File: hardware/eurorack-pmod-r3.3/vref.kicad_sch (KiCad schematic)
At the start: 8 parts, among them U8 LM4040DBZ-3 VREF, U9 TL072 OP AMP

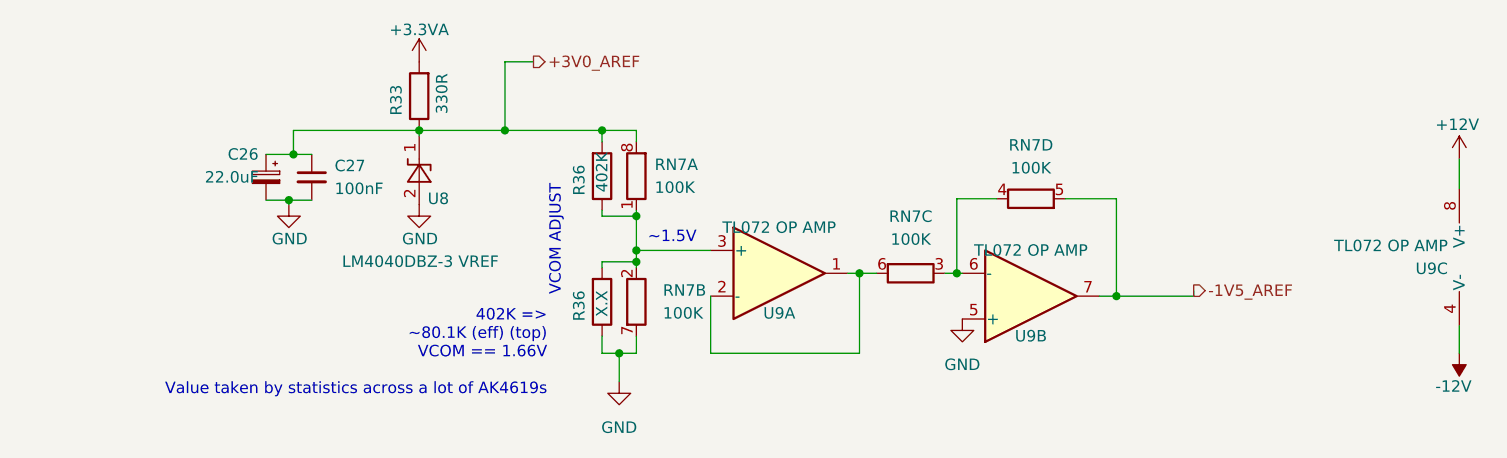
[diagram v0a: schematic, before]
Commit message: - Swap stackup s/4/6     - Was: GND/SIG/SIG/GND     - Now: GND/VDD/SIG/SIG/GND/GND - Swap CY8CMBR3108 for CY8CMBR3116     - Touch indices do NOT match previous revision.     - TODO revise new pinout (XRES) - Combine GNDD and GNDA     - Remove inductors between planes     - Mounting hole connects to GNDD / GNDA - Clean up traces now moved to VDD plane - Add EMC 33R series on SDOUT1
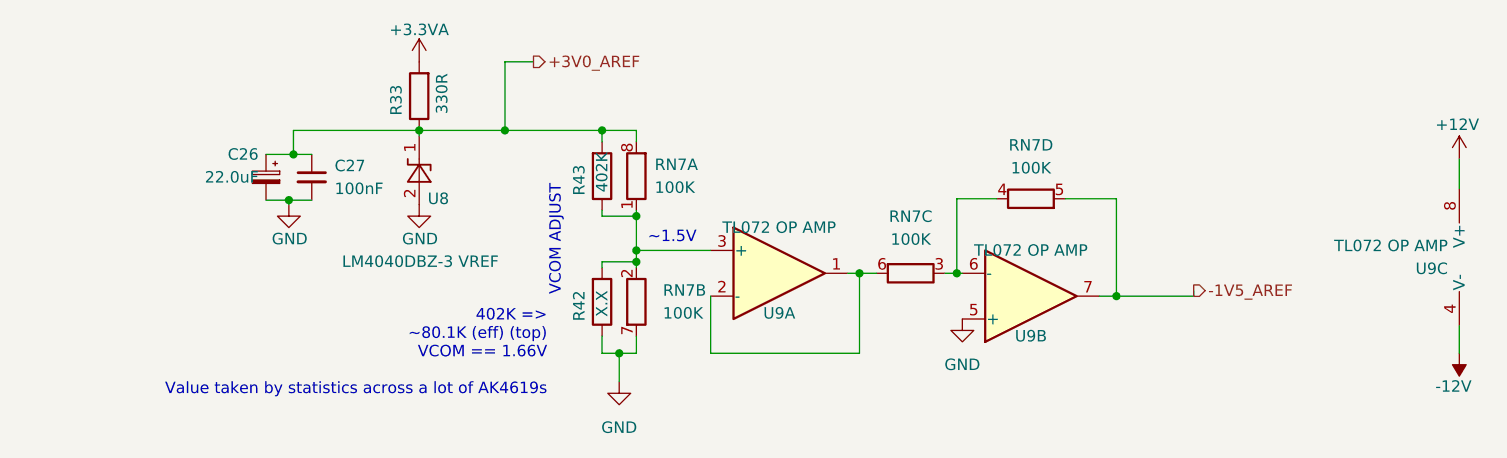
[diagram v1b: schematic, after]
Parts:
- renumbered R36 to R42, R36 to R43

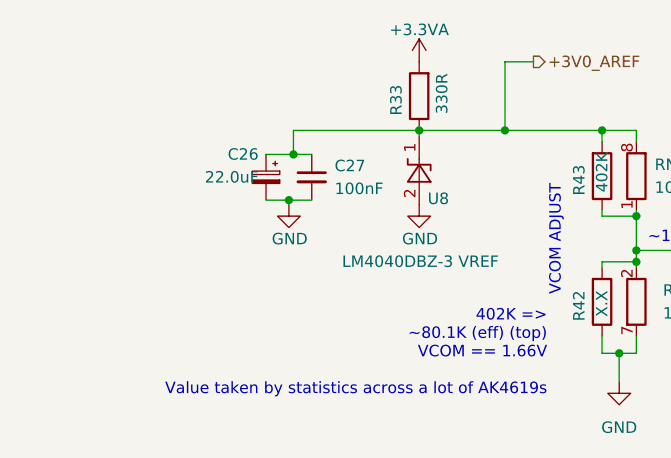
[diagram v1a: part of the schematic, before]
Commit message: - Swap all tantalums for ceramics
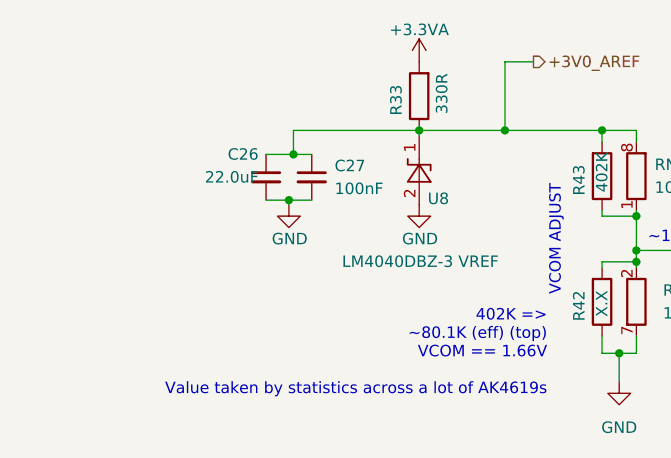
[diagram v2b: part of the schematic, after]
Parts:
- C26: footprint Capacitor_Tantalum_SMD:CP_EIA-3216-10_Kemet-I -> Capacitor_SMD:C_1206_3216Metric; symbol Device:C_Polarized_Small -> Device:C_Small; lcsc# C782264 -> C12891
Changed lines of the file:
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@@
 	)
 	(symbol
-		(lib_id "Device:C_Polarized_Small")
+		(lib_id "Device:C_Small")
 		(at 80.772 45.212 0)
 		(mirror y)
@@
 			)
 		)
-		(property "Footprint" "Capacitor_Tantalum_SMD:CP_EIA-3216-10_Kemet-I"
+		(property "Footprint" "Capacitor_SMD:C_1206_3216Metric"
 			(at 80.772 45.212 0)
 			(effects
@@
 			)
 		)
-		(property "Datasheet" ""
+		(property "Datasheet" "~"
 			(at 80.772 45.212 0)
 			(effects
@@
 			)
 		)
-		(property "Description" ""
+		(property "Description" "Unpolarized capacitor, small symbol"
 			(at 80.772 45.212 0)
 			(effects
@@
 					(size 1.27 1.27)
 				)
+				(hide yes)
 			)
 		)
@@
 			)
 		)
-		(property "lcsc#" "C782264"
+		(property "lcsc#" "C12891"
 			(at 80.772 45.212 0)
 			(effects

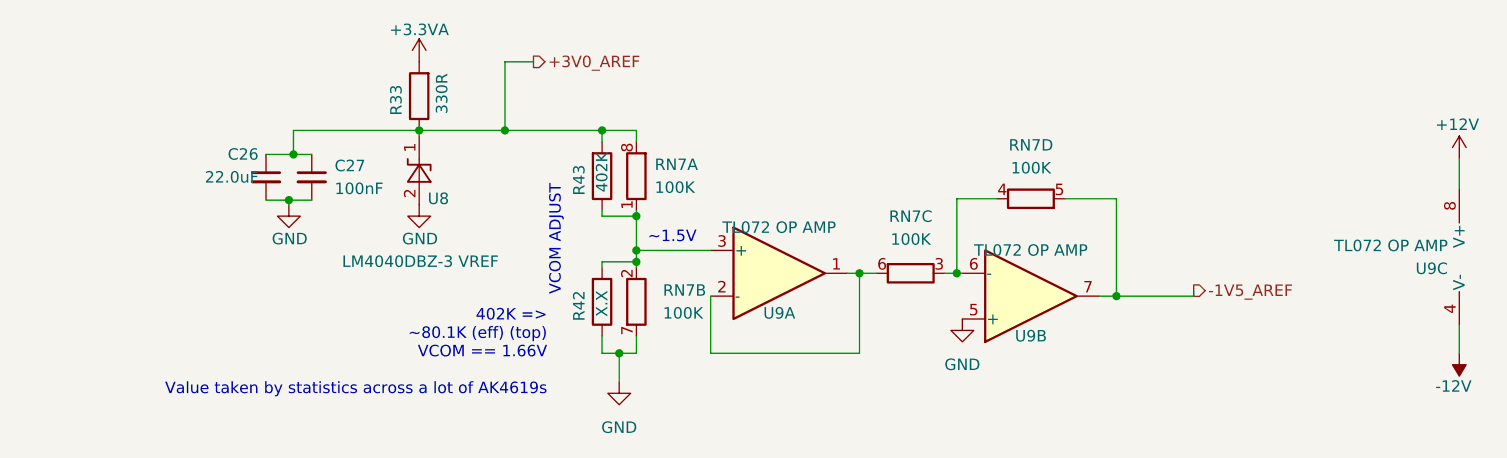
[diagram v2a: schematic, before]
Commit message: vref: replace +3.0V with local 12V->3.3V LDO
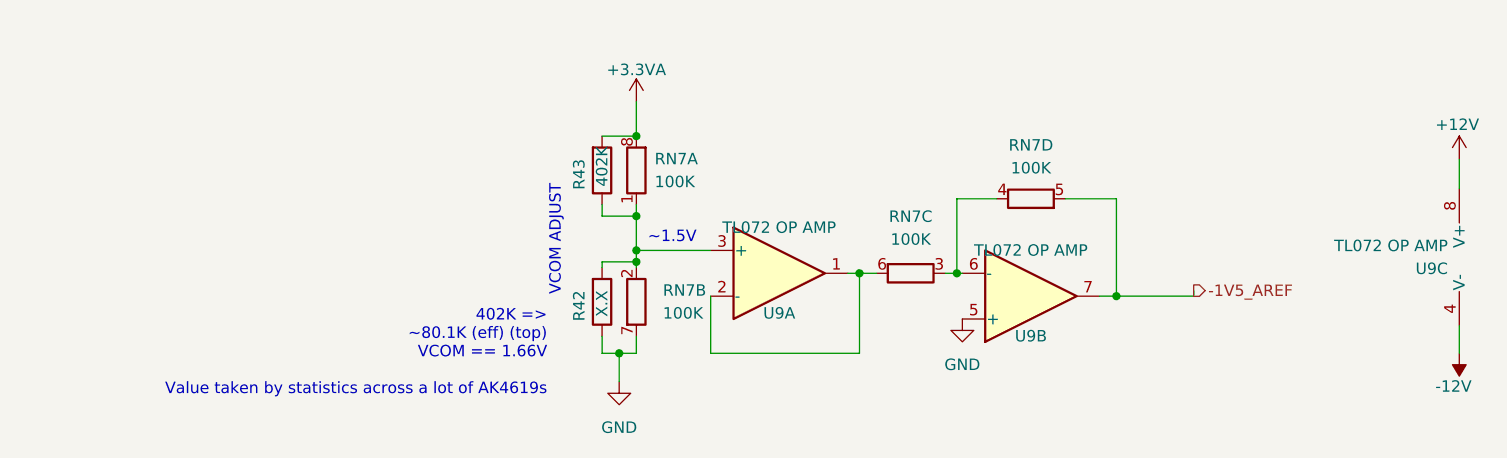
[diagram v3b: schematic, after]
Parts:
- removed C26: 22.0uF, Capacitor_SMD:C_1206_3216Metric, symbol Device:C_Small
- removed C27: 100nF, Capacitor_SMD:C_0603_1608Metric, symbol Device:C_Small
- removed R33: 330R, Resistor_SMD:R_0603_1608Metric, symbol Device:R
- removed U8: LM4040DBZ-3 VREF, Package_TO_SOT_SMD:SOT-23, symbol Reference_Voltage:LM4040DBZ-3
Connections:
- net +3V0_AREF is gone; now on net +3.3VA: R43.2, RN7.8 (R1.2)
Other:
- moved on the sheet: R43, RN7A

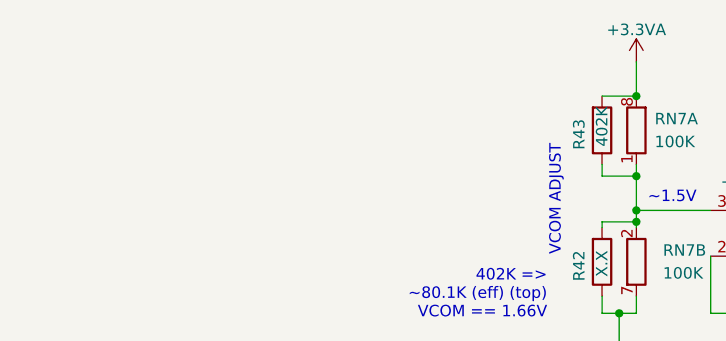
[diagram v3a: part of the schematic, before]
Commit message: place new parts
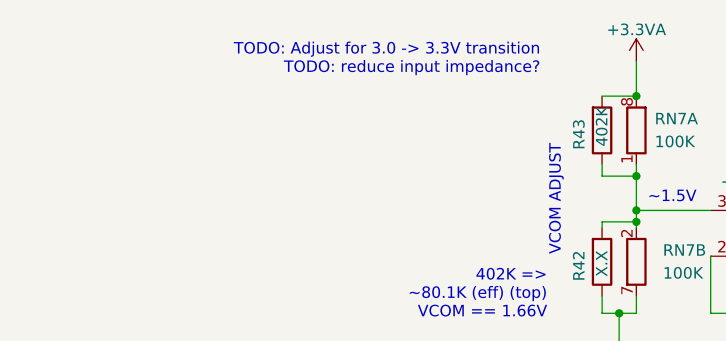
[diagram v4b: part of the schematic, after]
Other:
- note added: "TODO: Adjust for 3.0 -> 3.3V transition TODO: reduce input impedance?"
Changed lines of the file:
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@@
 	(generator_version "9.0")
 	(paper "A4")
+	(text "TODO: Adjust for 3.0 -> 3.3V transition\nTODO: reduce input impedance?"
+		(exclude_from_sim no)
+		(at 111.252 38.354 0)
+		(effects
+			(font
+				(size 1.27 1.27)
+			)
+			(justify right bottom)
+		)
+	)
 	(text "402K =>\n~80.1K (eff) (top)\nVCOM == 1.66V\n\nValue taken by statistics across a lot of AK4619s"
 		(exclude_from_sim no)

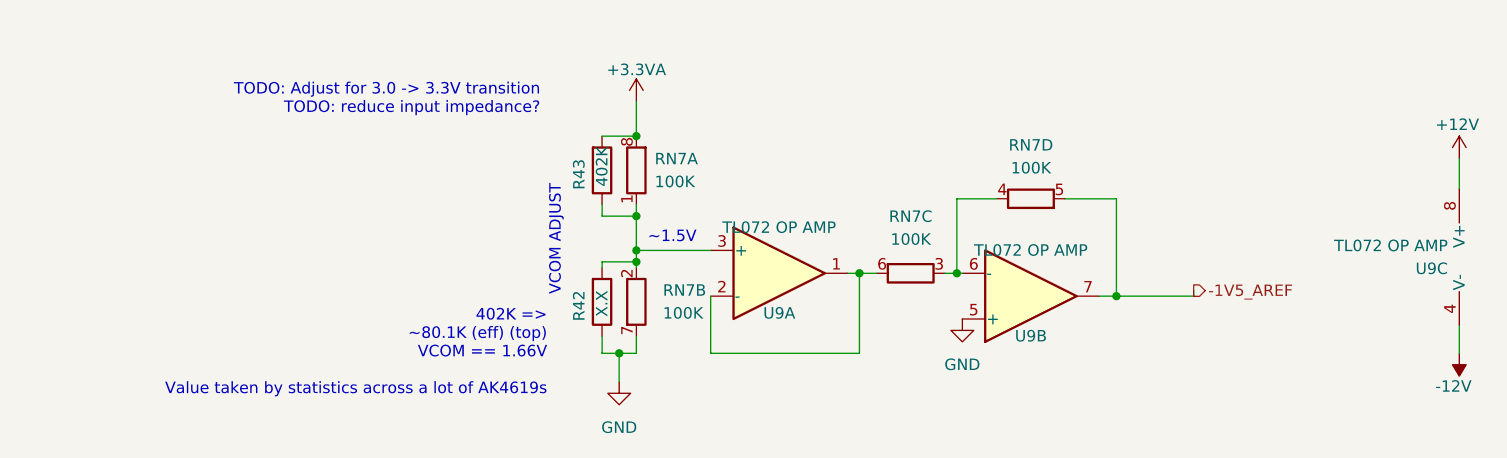
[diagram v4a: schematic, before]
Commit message: r3.5: add 100k output terminations and 100nF vref filtering, fab outputs (not sent yet)
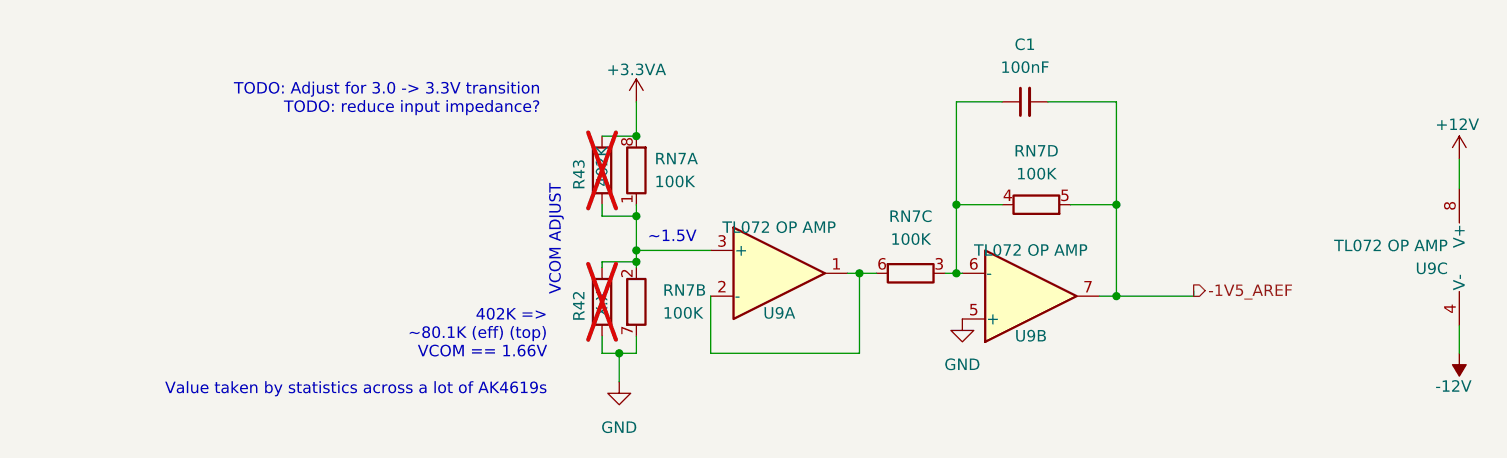
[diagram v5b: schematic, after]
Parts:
- added C1: 100nF, Capacitor_SMD:C_0603_1608Metric, symbol Device:C_Small
- R42, R43: now not fitted; now left out of the parts list
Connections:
- net -1V5_AREF: now also C1.2
- net at RN7.3 (R3.1), RN7.4 (R4.1), U9.6 (-): now also C1.1
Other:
- moved on the sheet: RN7D
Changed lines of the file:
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@@
+	)
+	(junction
+		(at 157.48 48.26)
+		(diameter 0)
+		(color 0 0 0 0)
 	)
 	(junction
@@
 	)
 	(junction
-		(at 121.92 53.34)
+		(at 157.48 55.88)
 		(diameter 0)
 		(color 0 0 0 0)
 	)
 	(junction
-		(at 157.5308 55.88)
+		(at 121.92 53.34)
 		(diameter 0)
 		(color 0 0 0 0)
@@
 		(color 0 0 0 0)
 	)
+	(junction
+		(at 175.26 48.26)
+		(diameter 0)
+		(color 0 0 0 0)
+	)
 	(wire
 		(pts
@@
 	(wire
 		(pts
+			(xy 162.56 36.83) (xy 157.48 36.83)
+		)
+		(stroke
+			(width 0)
+			(type default)
+		)
+	)
+	(wire
+		(pts
 			(xy 175.26 58.42) (xy 183.8452 58.42)
 		)
@@
 	(wire
 		(pts
+			(xy 157.48 36.83) (xy 157.48 48.26)
+		)
+		(stroke
+			(width 0)
+			(type default)
+		)
+	)
+	(wire
+		(pts
 			(xy 146.7104 55.88) (xy 148.59 55.88)
 		)
@@
 	(wire
 		(pts
+			(xy 175.26 36.83) (xy 175.26 48.26)
+		)
+		(stroke
+			(width 0)
+			(type default)
+		)
+	)
+	(wire
+		(pts
 			(xy 130.175 64.77) (xy 146.7104 64.77)
 		)
@@
 	(wire
 		(pts
+			(xy 167.64 36.83) (xy 175.26 36.83)
+		)
+		(stroke
+			(width 0)
+			(type default)
+		)
+	)
+	(wire
+		(pts
 			(xy 213.36 61.722) (xy 213.36 64.77)
 		)
@@
 	(wire
 		(pts
-			(xy 175.26 47.5996) (xy 175.26 58.42)
+			(xy 175.26 48.26) (xy 175.26 58.42)
 		)
 		(stroke
@@
 	(wire
 		(pts
+			(xy 157.48 55.88) (xy 158.1404 55.88)
+		)
+		(stroke
+			(width 0)
+			(type default)
+		)
+	)
+	(wire
+		(pts
 			(xy 173.3804 58.42) (xy 175.26 58.42)
 		)
@@
 	(wire
 		(pts
-			(xy 169.5704 47.5996) (xy 175.26 47.5996)
-		)
-		(stroke
-			(width 0)
-			(type default)
-		)
-	)
-	(wire
-		(pts
-			(xy 157.5308 55.88) (xy 158.1404 55.88)
+			(xy 170.18 48.26) (xy 175.26 48.26)
 		)
 		(stroke
@@
 	(wire
 		(pts
-			(xy 157.5308 47.5996) (xy 161.9504 47.5996)
-		)
-		(stroke
-			(width 0)
-			(type default)
-		)
-	)
-	(wire
-		(pts
-			(xy 156.21 55.88) (xy 157.5308 55.88)
+			(xy 157.48 48.26) (xy 162.56 48.26)
+		)
+		(stroke
+			(width 0)
+			(type default)
+		)
+	)
+	(wire
+		(pts
+			(xy 156.21 55.88) (xy 157.48 55.88)
 		)
 		(stroke
@@
 	(wire
 		(pts
-			(xy 157.5308 47.5996) (xy 157.5308 55.88)
+			(xy 157.48 48.26) (xy 157.48 55.88)
 		)
 		(stroke
@@
 		(unit 1)
 		(exclude_from_sim no)
-		(in_bom yes)
-		(on_board yes)
-		(dnp no)
+		(in_bom no)
+		(on_board no)
+		(dnp yes)
 		(property "Reference" "R42"
 			(at 115.57 57.785 90)
@@
 		(unit 1)
 		(exclude_from_sim no)
-		(in_bom yes)
-		(on_board yes)
-		(dnp no)
+		(in_bom no)
+		(on_board no)
+		(dnp yes)
 		(property "Reference" "R43"
 			(at 115.57 43.18 90)
@@
 	)
 	(symbol
+		(lib_id "Device:C_Small")
+		(at 165.1 36.83 90)
+		(mirror x)
+		(unit 1)
+		(exclude_from_sim no)
+		(in_bom yes)
+		(on_board yes)
+		(dnp no)
+		(fields_autoplaced yes)
+		(property "Reference" "C1"
+			(at 165.1063 30.48 90)
+			(effects
+				(font
+					(size 1.27 1.27)
+				)
+			)
+		)
+		(property "Value" "100nF"
+			(at 165.1063 33.02 90)
+			(effects
+				(font
+					(size 1.27 1.27)
+				)
+			)
+		)
+		(property "Footprint" "Capacitor_SMD:C_0603_1608Metric"
+			(at 165.1 36.83 0)
+			(effects
+				(font
+					(size 1.27 1.27)
+				)
+				(hide yes)
+			)
+		)
+		(property "Datasheet" "https://datasheet.lcsc.com/lcsc/1912111437_TDK-C1608X7R1E104KT000N_C338036.pdf"
+			(at 165.1 36.83 0)
+			(effects
+				(font
+					(size 1.27 1.27)
+				)
+				(hide yes)
+			)
+		)
+		(property "Description" ""
+			(at 165.1 36.83 0)
+			(effects
+				(font
+					(size 1.27 1.27)
+				)
+			)
+		)
+		(property "lcsc#" "C338036"
+			(at 165.1 36.83 0)
+			(effects
+				(font
+					(size 1.27 1.27)
+				)
+				(hide yes)
+			)
+		)
+		(property "mfg#" "C1608X7R1E104KT000N"
+			(at 165.1 36.83 0)
+			(effects
+				(font
+					(size 1.27 1.27)
+				)
+				(hide yes)
+			)
+		)
+		(pin "1"
+		)
+		(pin "2"
+		)
+		(instances
+			(project "eurorack-pmod-pcb"
+				(path "/d1469efb-590b-4a61-a37b-5bbc286936ba/04b0c562-7287-43d3-9594-fcf167d8f492"
+					(reference "C1")
+					(unit 1)
+				)
+			)
+		)
+	)
+	(symbol
 		(lib_id "Device:R_Pack04_Split")
-		(at 165.7604 47.5996 270)
+		(at 166.37 48.26 270)
 		(unit 4)
 		(exclude_from_sim no)
@@
 		(fields_autoplaced yes)
 		(property "Reference" "RN7"
-			(at 165.7604 41.656 90)
+			(at 166.37 42.3164 90)
 			(effects
 				(font
@@
 		)
 		(property "Value" "100K"
-			(at 165.7604 44.196 90)
+			(at 166.37 44.8564 90)
 			(effects
 				(font
@@
 		)
 		(property "Footprint" "Resistor_SMD:R_Array_Convex_4x0402"
-			(at 165.7604 45.5676 90)
+			(at 166.37 46.228 90)
 			(effects
 				(font
@@
 		)
 		(property "Datasheet" "https://datasheet.lcsc.com/lcsc/1811141451_YAGEO-YC124-FR-07100KL_C326786.pdf"
-			(at 165.7604 47.5996 0)
+			(at 166.37 48.26 0)
 			(effects
 				(font
@@
 		)
 		(property "Description" ""
-			(at 165.7604 47.5996 0)
+			(at 166.37 48.26 0)
 			(effects
 				(font
@@
 		)
 		(property "dig#" ""
-			(at 165.7604 51.816 90)
+			(at 166.37 52.4764 90)
 			(effects
 				(font
@@
 		)
 		(property "mfg#" "YC124-FR-07100KL"
-			(at 165.7604 54.356 90)
+			(at 166.37 55.0164 90)
 			(effects
 				(font
@@
 		)
 		(property "lcsc#" "C326786"
-			(at 165.7604 47.5996 0)
-			(effects
-				(font
+			(at 166.37 48.26 0)
+			(effects
+				(font

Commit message: r3.5: update part numbers and fab
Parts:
- R43: value 402K -> X.X; lcsc# C327345 -> (none); mfg# RC0402FR-07402KL -> (none)
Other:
- note removed: "402K => ~80.1K (eff) (top) VCOM == 1.66V Value taken by statistics across a lot of AK4619s"
- note removed: "TODO: Adjust for 3.0 -> 3.3V transition TODO: reduce input impedance?"
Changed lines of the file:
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@@
 	(generator_version "9.0")
 	(paper "A4")
-	(text "TODO: Adjust for 3.0 -> 3.3V transition\nTODO: reduce input impedance?"
-		(exclude_from_sim no)
-		(at 111.252 38.354 0)
-		(effects
-			(font
-				(size 1.27 1.27)
-			)
-			(justify right bottom)
-		)
-	)
-	(text "402K =>\n~80.1K (eff) (top)\nVCOM == 1.66V\n\nValue taken by statistics across a lot of AK4619s"
-		(exclude_from_sim no)
-		(at 112.014 69.596 0)
-		(effects
-			(font
-				(size 1.27 1.27)
-			)
-			(justify right bottom)
-		)
-	)
 	(text "~1.5V"
 		(exclude_from_sim no)
@@
 			)
 		)
-		(property "Value" "402K"
+		(property "Value" "X.X"
 			(at 118.11 41.783 90)
 			(effects
@@
 			)
 		)
-		(property "lcsc#" "C327345"
+		(property "lcsc#" ""
 			(at 118.11 44.45 0)
 			(effects
@@
 			)
 		)
-		(property "mfg#" "RC0402FR-07402KL"
+		(property "mfg#" ""
 			(at 118.11 44.45 0)
 			(effects
